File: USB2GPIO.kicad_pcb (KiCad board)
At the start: 2 copper layers, 52.3 x 21.1 mm, 39 parts, among them J1 Conn_01x04, J7 Conn_01x03, J8 Conn_01x03, J9 Conn_01x04, Q1 S8050, U10 PCF8574, U11 HX9193, U12 SL2.1S, U2 CH340E, U3 CH340E, U9 ATtiny85V-10S, Y2 12M

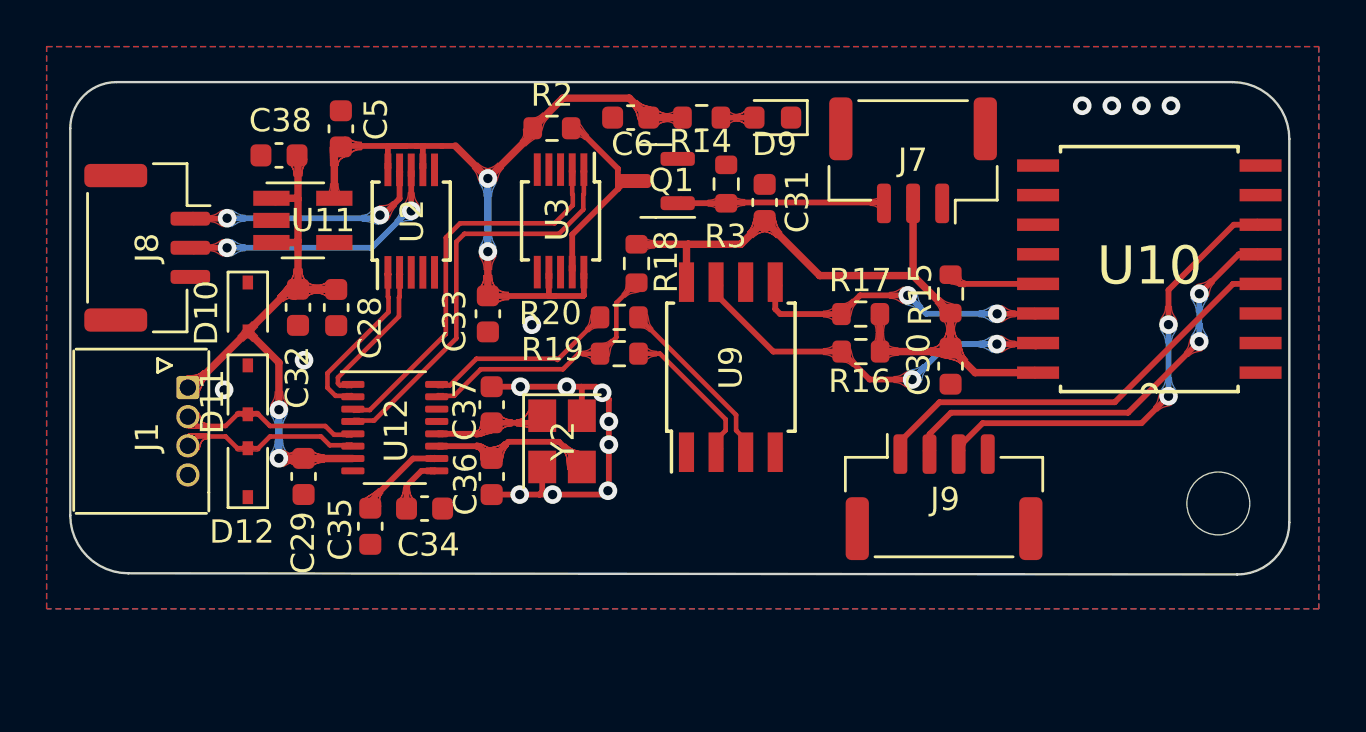
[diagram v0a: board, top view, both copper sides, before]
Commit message: Change footprint of MX1.25 and change some routings and silkscreens
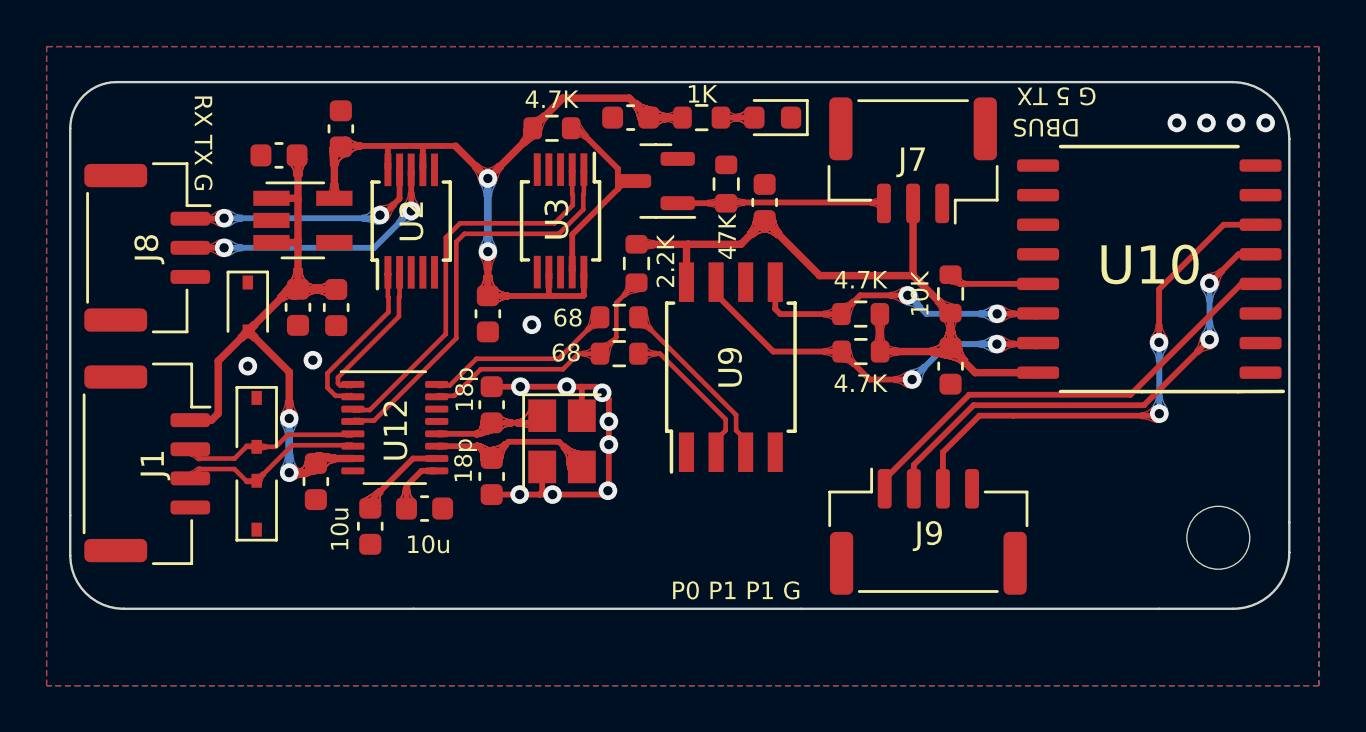
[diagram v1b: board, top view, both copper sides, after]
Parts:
- J1: footprint Connector_JST:JST_EH_S4B-EH_1x04_P2.50mm_Horizontal -> Connector_Molex:Molex_CLIK-Mate_502386-0470_1x04-1MP_P1.25mm_Horizontal
- moved J1 3.71 mm to (42.4, 138.6)
- moved J9 1.63 mm to (75.9, 141.5)
- moved H1 1.47 mm to (88.4, 141.7)
- moved D12 1.45 mm to (47.1, 140.3)
- moved D11 1.45 mm to (47.1, 136.8)
- moved C29 0.57 mm to (49.7, 139.3)
- renumbered R15 to 10K, C35 to 10u, C34 to 10u, C37 to 18p, C36 to 18p, R14 to 1K, R18 to 2.2K, R16 to 4.7K, R17 to 4.7K, R2 to 4.7K, R3 to 47K, R20 to 68, R19 to 68
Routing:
- net /GPIO/P2: track 19.9 -> 22.4 mm
- net +5V: track 25.4 -> 27.9 mm
- net /GPIO/P1: track 19.5 -> 21.1 mm
- net /GPIO/P0: track 18.8 -> 20.0 mm
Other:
- board size 52.3 x 21.1 mm -> 52.3 x 22.6 mm
- board text added: "DBUS"
- board text added: "G 5 TX"
- board text added: "P0 P1 P1 G"
- board text added: "RX TX G"

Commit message: Change '5V' tag to '+5V' net
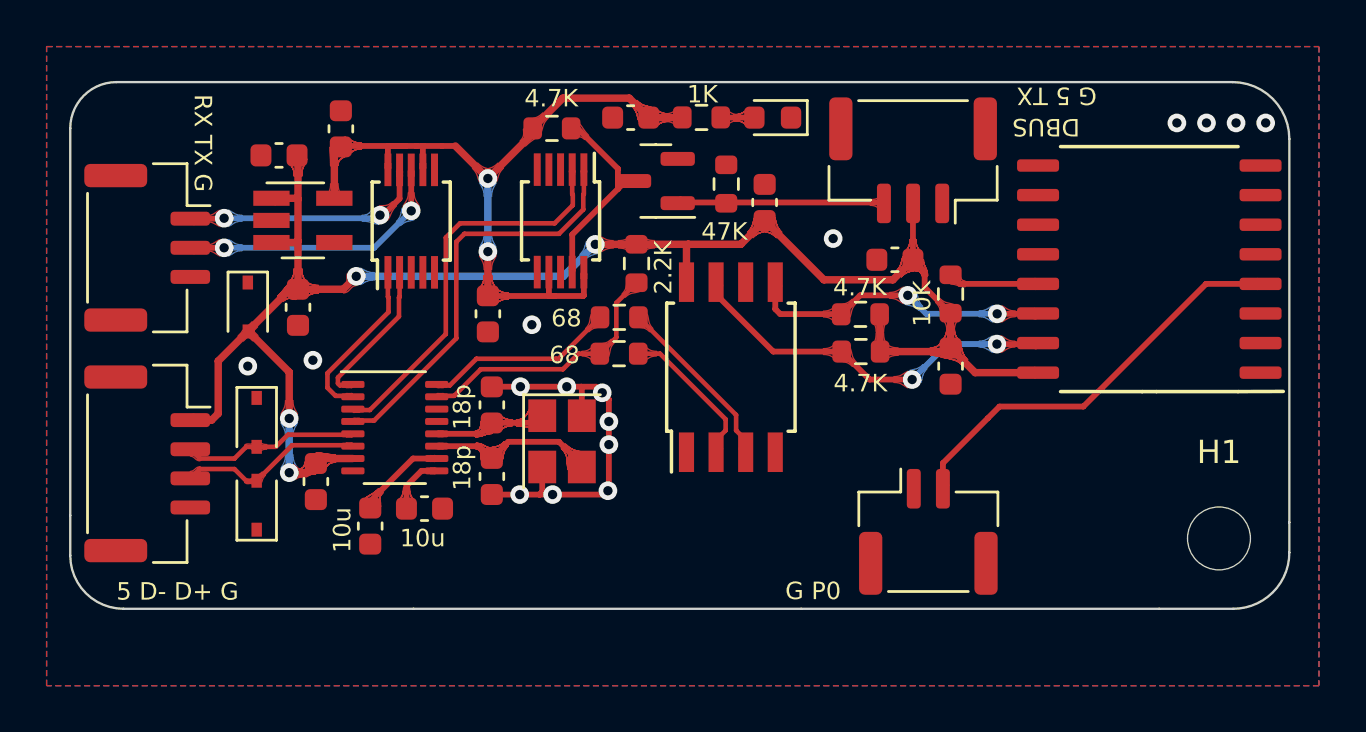
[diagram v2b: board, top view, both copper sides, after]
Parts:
- removed 10K: 10K, Resistor_SMD:R_0603_1608Metric
- removed 10u (x2): 10u, Capacitor_SMD:C_0603_1608Metric
- removed 18p (x2): 18p, Capacitor_SMD:C_0603_1608Metric
- removed 1K: 1K, Resistor_SMD:R_0603_1608Metric
- removed 2.2K: 2.2K, Resistor_SMD:R_0603_1608Metric
- removed 4.7K (x3): 4.7K, Resistor_SMD:R_0603_1608Metric
- removed 47K: 47K, Resistor_SMD:R_0603_1608Metric
- removed 68 (x2): 68, Resistor_SMD:R_0603_1608Metric
- added C34: 10u, Capacitor_SMD:C_0603_1608Metric, F.Cu at (54.3, 140.5)
- added C35: 10u, Capacitor_SMD:C_0603_1608Metric, F.Cu at (52.0, 141.2)
- added C36: 18p, Capacitor_SMD:C_0603_1608Metric, F.Cu at (57.2, 139.1)
- added C37: 18p, Capacitor_SMD:C_0603_1608Metric, F.Cu at (57.2, 136.0)
- added R14: 1K, Resistor_SMD:R_0603_1608Metric, F.Cu at (66.2, 123.7)
- added R15: 10K, Resistor_SMD:R_0603_1608Metric, F.Cu at (76.9, 131.3)
- added R16: 4.7K, Resistor_SMD:R_0603_1608Metric, F.Cu at (73.0, 133.7)
- added R17: 4.7K, Resistor_SMD:R_0603_1608Metric, F.Cu at (73.0, 132.1)
- added R18: 2.2K, Resistor_SMD:R_0603_1608Metric, F.Cu at (63.4, 130.0)
- added R19: 68, Resistor_SMD:R_0603_1608Metric, F.Cu at (62.7, 133.8)
- added R2: 4.7K, Resistor_SMD:R_0603_1608Metric, F.Cu at (59.8, 124.2)
- added R20: 68, Resistor_SMD:R_0603_1608Metric, F.Cu at (62.7, 132.3)
- added R3: 47K, Resistor_SMD:R_0603_1608Metric, F.Cu at (67.3, 126.5)
- J1: footprint Connector_Molex:Molex_CLIK-Mate_502386-0470_1x04-1MP_P1.25mm_Horizontal -> Connector_JST:JST_GH_SM04B-GHS-TB_1x04-1MP_P1.25mm_Horizontal
- J9: value Conn_01x04 -> Conn_01x02; footprint Connector_JST:JST_GH_SM04B-GHS-TB_1x04-1MP_P1.25mm_Horizontal -> Connector_JST:JST_GH_SM02B-GHS-TB_1x02-1MP_P1.25mm_Horizontal
- moved C28 24.1 mm to (74.5, 129.8), turned to 180 degrees
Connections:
- C30 pad 1: /5V -> +5V
- C31 pad 1: /5V -> +5V
- J7 pad 2: /5V -> +5V
- J9 pad 1: /GPIO/P0 -> GND
- J9 pad 2: /GPIO/P1 -> /GPIO/P0
- U10 pad 16: /5V -> +5V
- U9 pad 8: /5V -> +5V
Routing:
- net +5V: track 27.9 -> 72.3 mm, vias 2 -> 4
- net /5V: track 30.7 -> 0.00 mm
- net /GPIO/P2: track 22.4 -> 0.00 mm, vias 2 -> 0
- net /GPIO/P1: track 21.1 -> 0.00 mm, vias 2 -> 0
- net /GPIO/P0: track 20.0 -> 17.9 mm
- net GND: vias 15 -> 16
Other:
- board text added: "10K"
- board text added: "10u"
- board text added: "18p"
- board text added: "1K"
- board text added: "2.2K"
- board text added: "4.7K"
- board text added: "47K"
- board text added: "5 D- D+ G"
- board text added: "68"
- board text added: "G P0"
- board text removed: "P0 P1 P1 G"

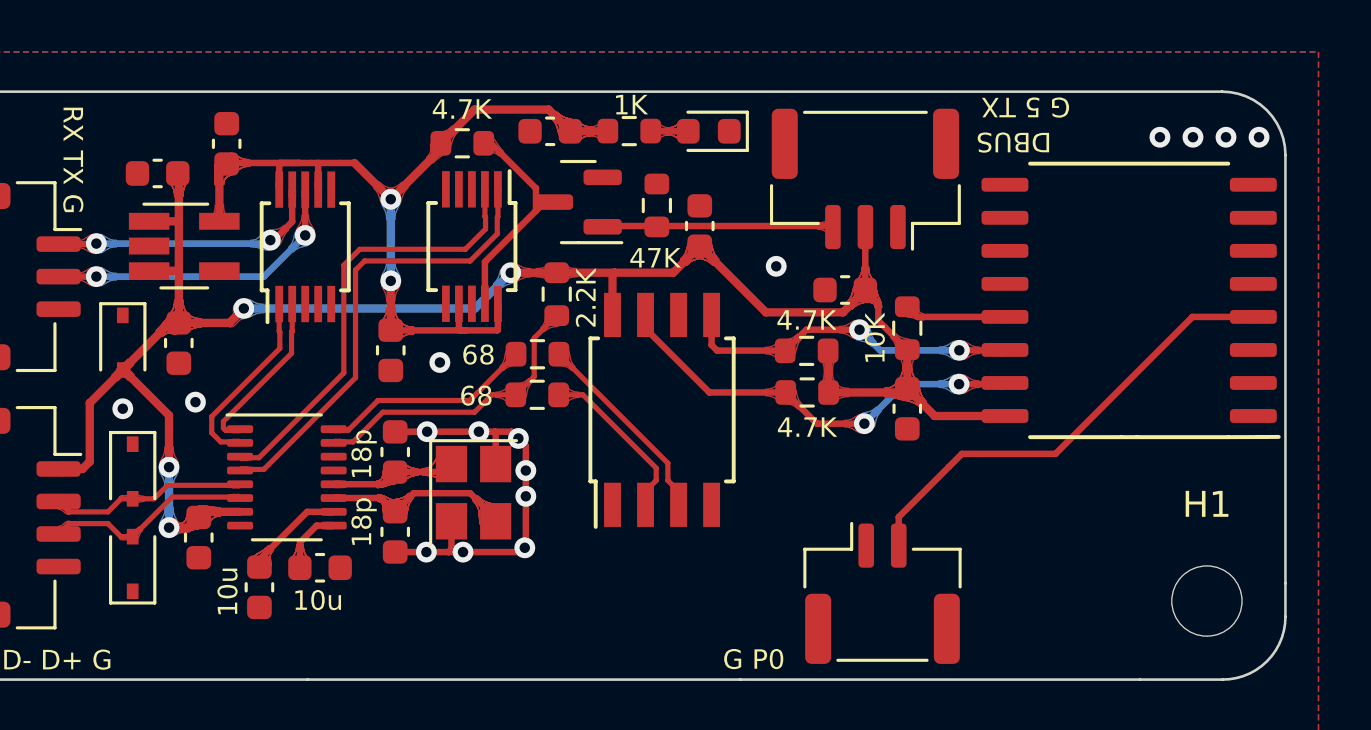
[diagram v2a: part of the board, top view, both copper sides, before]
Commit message: Change gpio-pin from P0 to P1
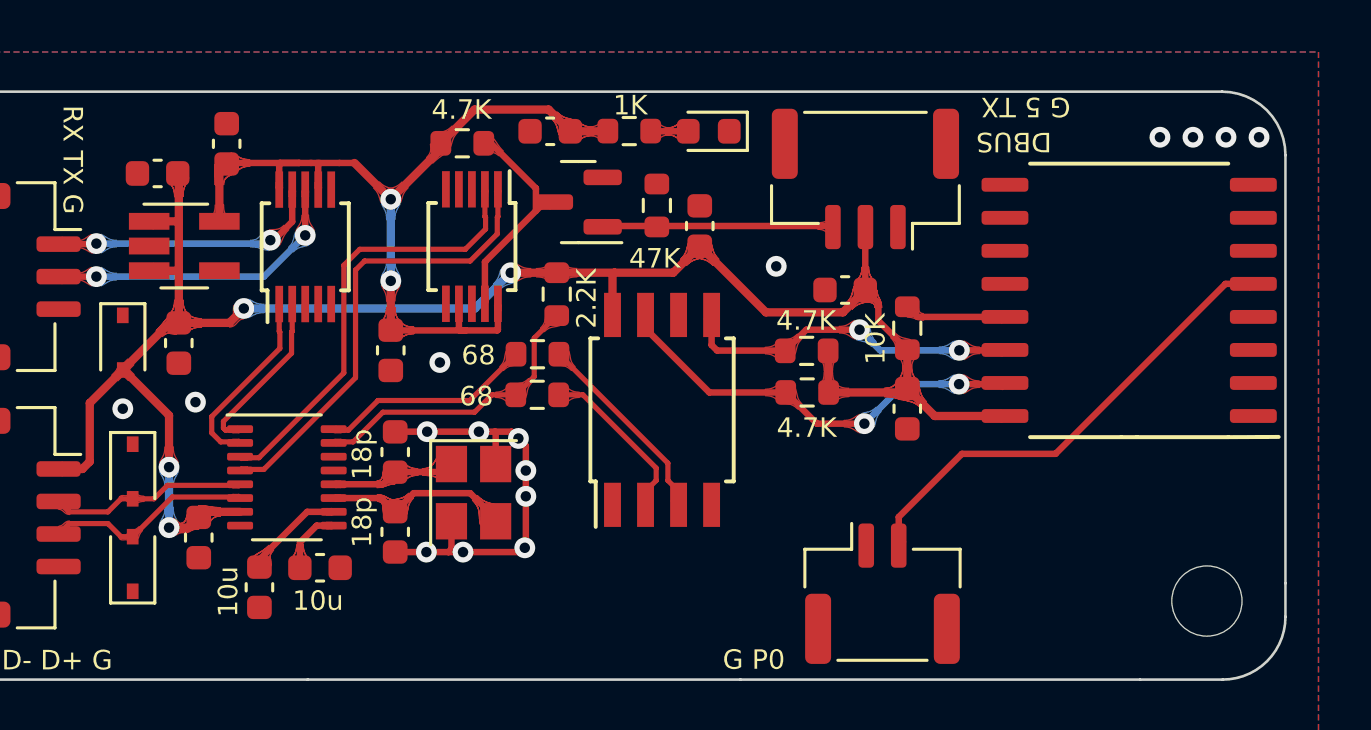
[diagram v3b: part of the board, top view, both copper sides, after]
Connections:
- J9 pad 2: /GPIO/P0 -> /GPIO/P1
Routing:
- net /GPIO/P1: track 0.00 -> 18.4 mm
- net /GPIO/P0: track 17.9 -> 0.00 mm

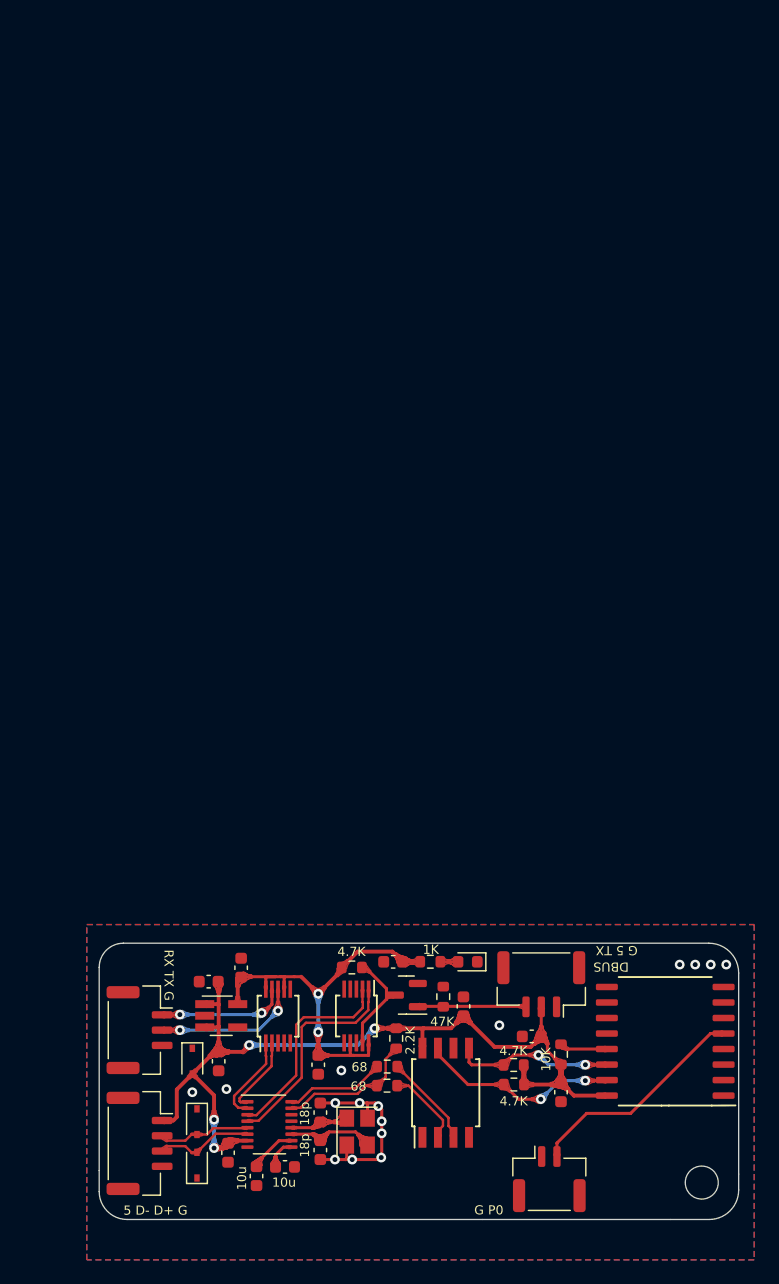
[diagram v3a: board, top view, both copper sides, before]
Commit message: Change the map and rebuild the PCB
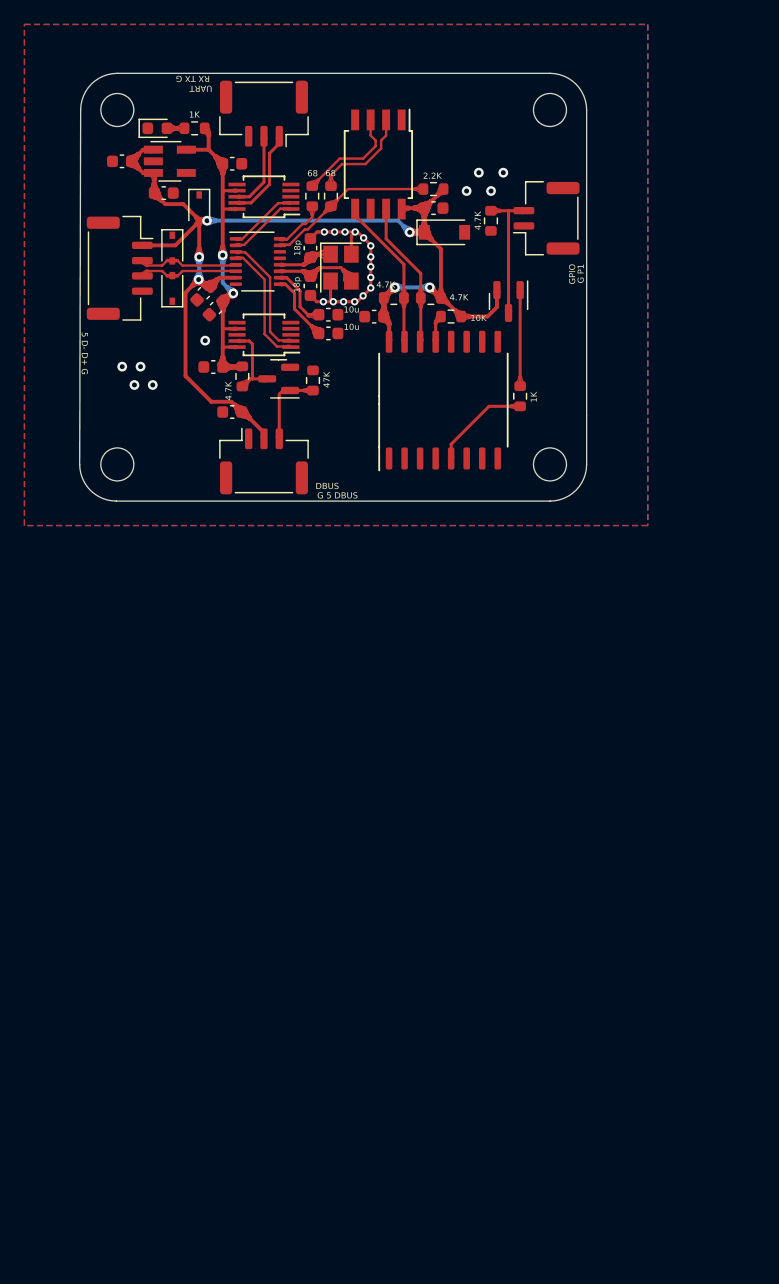
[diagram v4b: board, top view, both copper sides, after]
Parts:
- removed C6: 100n, Capacitor_SMD:C_0603_1608Metric
- added C7: 100n, Capacitor_SMD:C_0603_1608Metric, F.Cu at (48.7, 70.2)
- added D13: 5V1, Diode_SMD:D_SOD-123, F.Cu at (67.4, 64.0)
- added H2: MountingHole, MountingHole:MountingHole_2.7mm_M2.5, F.Cu at (76.0, 54.0)
- added H3: MountingHole, MountingHole:MountingHole_2.7mm_M2.5, F.Cu at (40.6, 83.0)
- added H4: MountingHole, MountingHole:MountingHole_2.7mm_M2.5, F.Cu at (40.6, 54.0)
- added Q10: Q_PNP_BEC, Package_TO_SOT_SMD:SOT-23, F.Cu at (72.6, 69.7)
- added R30: 1K, Resistor_SMD:R_0603_1608Metric, F.Cu at (73.6, 77.4)
- added R31: 4.7K, Resistor_SMD:R_0603_1608Metric, F.Cu at (71.2, 63.1)
- U10: value PCF8574 -> PCA9554D
- moved C28 79.1 mm to (41.0, 58.2)
- moved C29 78.7 mm to (44.4, 60.8), turned to 0 degrees
- moved J9 78.6 mm to (75.7, 62.9), turned to 90 degrees
- moved U9 76.1 mm to (62.0, 58.5), turned to -90 degrees
- moved J8 75.7 mm to (52.6, 54.3), turned to 180 degrees
- moved R19 72.9 mm to (58.1, 61.0), turned to -90 degrees
- moved D9 72.8 mm to (43.9, 55.5), turned to 0 degrees
- moved D12 71.8 mm to (45.1, 68.6)
- moved J1 71.6 mm to (40.8, 67.0)
- moved D11 71.5 mm to (45.1, 65.3)
- moved R20 71.5 mm to (56.5, 61.0), turned to -90 degrees
- moved R14 70.9 mm to (46.9, 55.5), turned to 180 degrees
- moved C37 70.7 mm to (56.4, 65.3)
- moved C35 70.7 mm to (57.9, 70.8), turned to 0 degrees
- moved Y2 70.7 mm to (58.9, 66.9)
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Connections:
- U10 pad 5: /GPIO/P1 -> Net-(R30-Pad2)
- U9 pad 5: /GPIO/SCL -> /GPIO/SDA
- U9 pad 7: /GPIO/SDA -> /GPIO/SCL
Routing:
- net +5V: track 72.3 -> 89.1 mm, vias 4 -> 6
- net Net-(R30-Pad2): track 0.00 -> 8.10 mm
- net Net-(Q10-Pad1): track 0.00 -> 7.86 mm
- net /DBUS/D+: track 17.8 -> 10.2 mm
- net /GPIO/P1: track 18.4 -> 11.1 mm
- net /DBUS/D-: track 17.1 -> 10.2 mm
- net /UART/TXD: track 12.0 -> 6.45 mm, vias 2 -> 0
- net /3V3: track 33.9 -> 29.2 mm
- net /GPIO/SDA: track 16.5 -> 12.5 mm, vias 2 -> 0
- net /GPIO/D+: track 8.28 -> 4.76 mm
- net /UART/RXD: track 10.8 -> 7.54 mm, vias 2 -> 0
- net Net-(C34-Pad1): track 2.54 -> 5.61 mm
- net /GPIO/D-: track 11.5 -> 14.3 mm
- net /DBUS/DBus: track 8.88 -> 6.54 mm
- net Net-(Q1-Pad3): track 8.80 -> 6.50 mm
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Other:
- board size 52.3 x 22.6 mm -> 41.5 x 35 mm
- board text added: "G 5 DBUS"
- board text added: "G P1"
- board text added: "GPIO"
- board text added: "UART"
- board text removed: "G 5 TX"
- board text removed: "G P0"
